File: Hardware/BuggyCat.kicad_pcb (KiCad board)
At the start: 2 copper layers, 51.2 x 124.2 mm, 106 parts, among them J1 Antenna, J2 BG306-02-A-2-0400-L-G, J3 Header7, J4 Header 2, J5 Header 4, J6 Input Power:2x AA Battery, P1 USB_C_Plug_USB2.0, Q1 AO3422, Q2 AO3422, Q3 LDA111STR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

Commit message: move logo
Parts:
- removed kibuzzard-642E0F9F: G***, kibuzzard-642E0F9F
- G***, kibuzzard-642E0AC9, kibuzzard-642E0AD5, kibuzzard-642E0AF5, kibuzzard-642E0B26, kibuzzard-642E0B82, kibuzzard-642E0B91: moved to F.Cu
- moved G*** 39.3 mm to (121.2, 71.0), turned to 0 degrees
- moved REF** 12.9 mm to (109.7, 119.0)
- moved G*** 8.86 mm to (102.3, 70.1)
- turned kibuzzard-642E0AC9 to 0 degrees
- turned kibuzzard-642E0AD5 to 0 degrees
- turned kibuzzard-642E0AF5 to 0 degrees
- turned kibuzzard-642E0B26 to 0 degrees
- turned kibuzzard-642E0B82 to 0 degrees
- turned kibuzzard-642E0B91 to 0 degrees

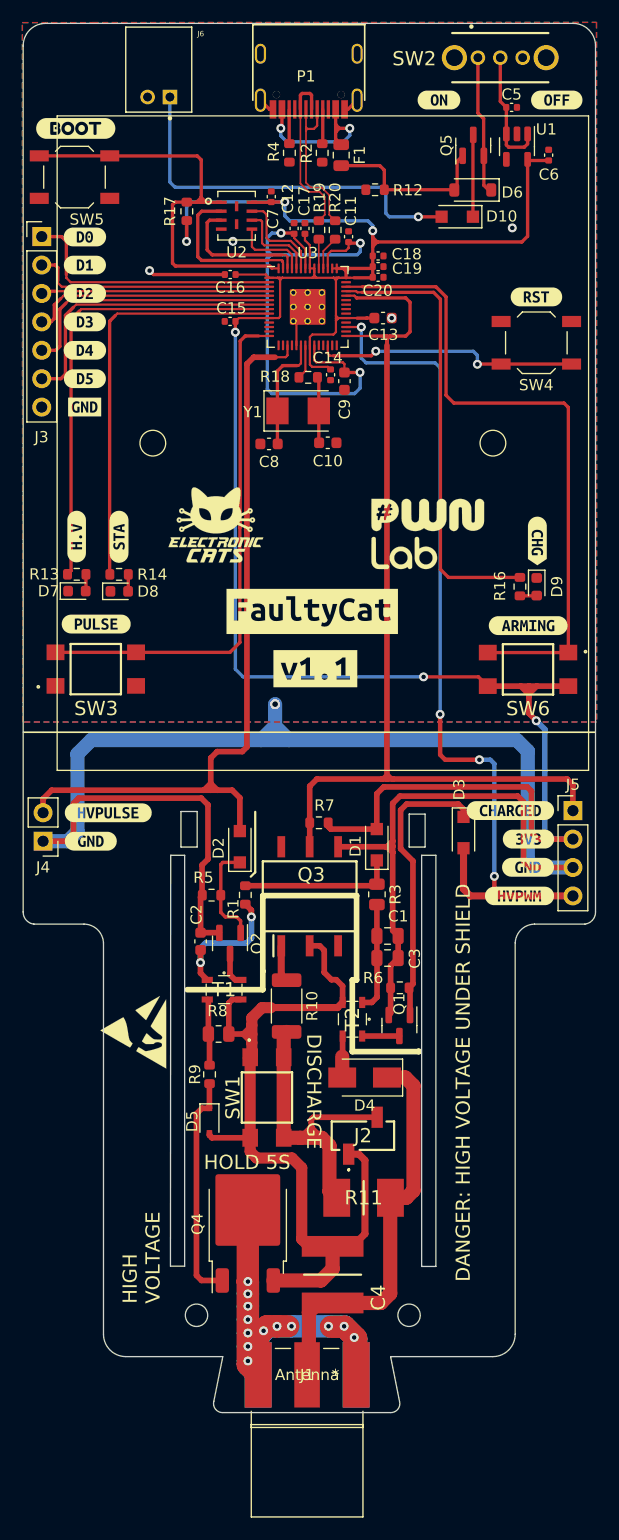
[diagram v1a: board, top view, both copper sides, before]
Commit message: Footprint of battery holder modified and J6 changed
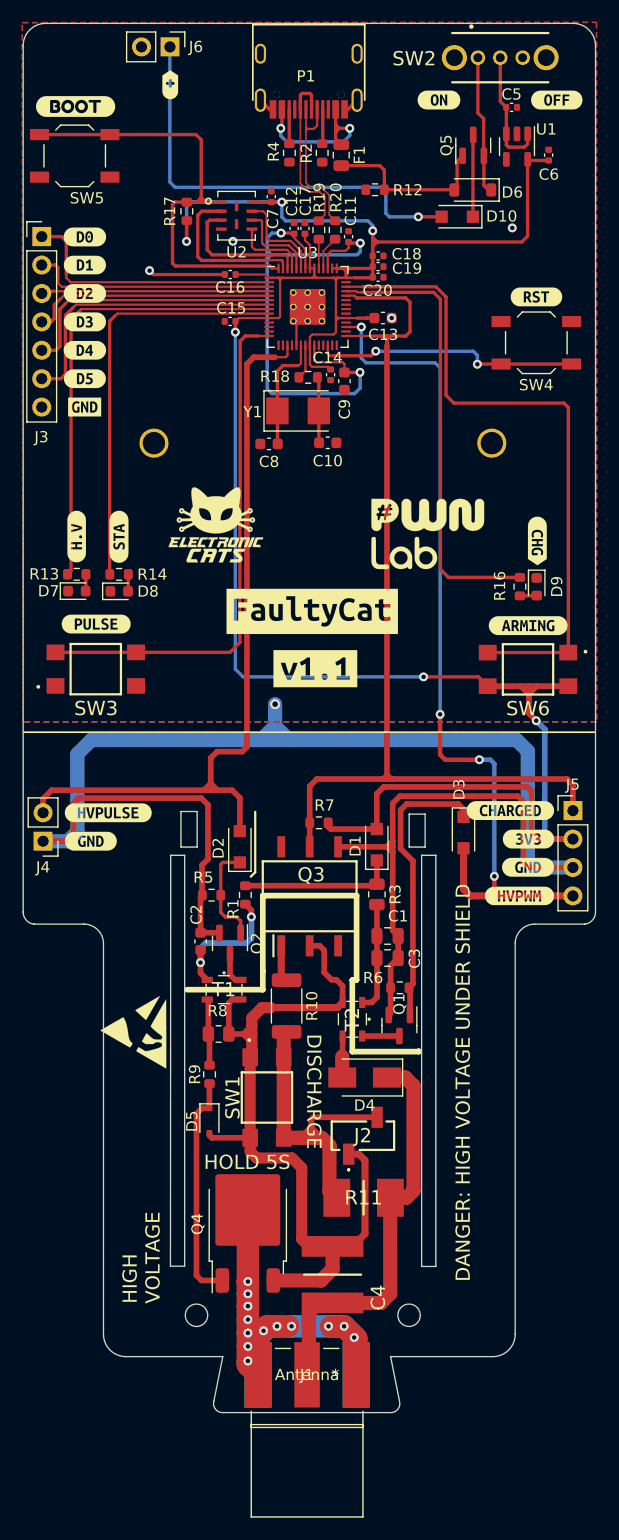
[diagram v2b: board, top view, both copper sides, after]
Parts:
- added kibuzzard-64767B55: G***, kibuzzard-64767B55, F.Cu at (98.2, 30.8)
- J6: footprint BuggyCat:JST_S2B-PH-K-S(LF)(SN) -> Connector_PinHeader_2.54mm:PinHeader_1x02_P2.54mm_Vertical
- moved J6 4.59 mm to (98.2, 27.4), turned to -90 degrees
- moved kibuzzard-642DF5C4 1.96 mm to (89.7, 32.7)
- moved SW5 1.90 mm to (89.7, 37.1)
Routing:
- net Net-(D10-A): track 34.3 -> 38.8 mm
- net /QSPI_CS: track 39.0 -> 40.8 mm
